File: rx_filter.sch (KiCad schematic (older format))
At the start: 12 parts, among them U10 LM339, U16 TL084

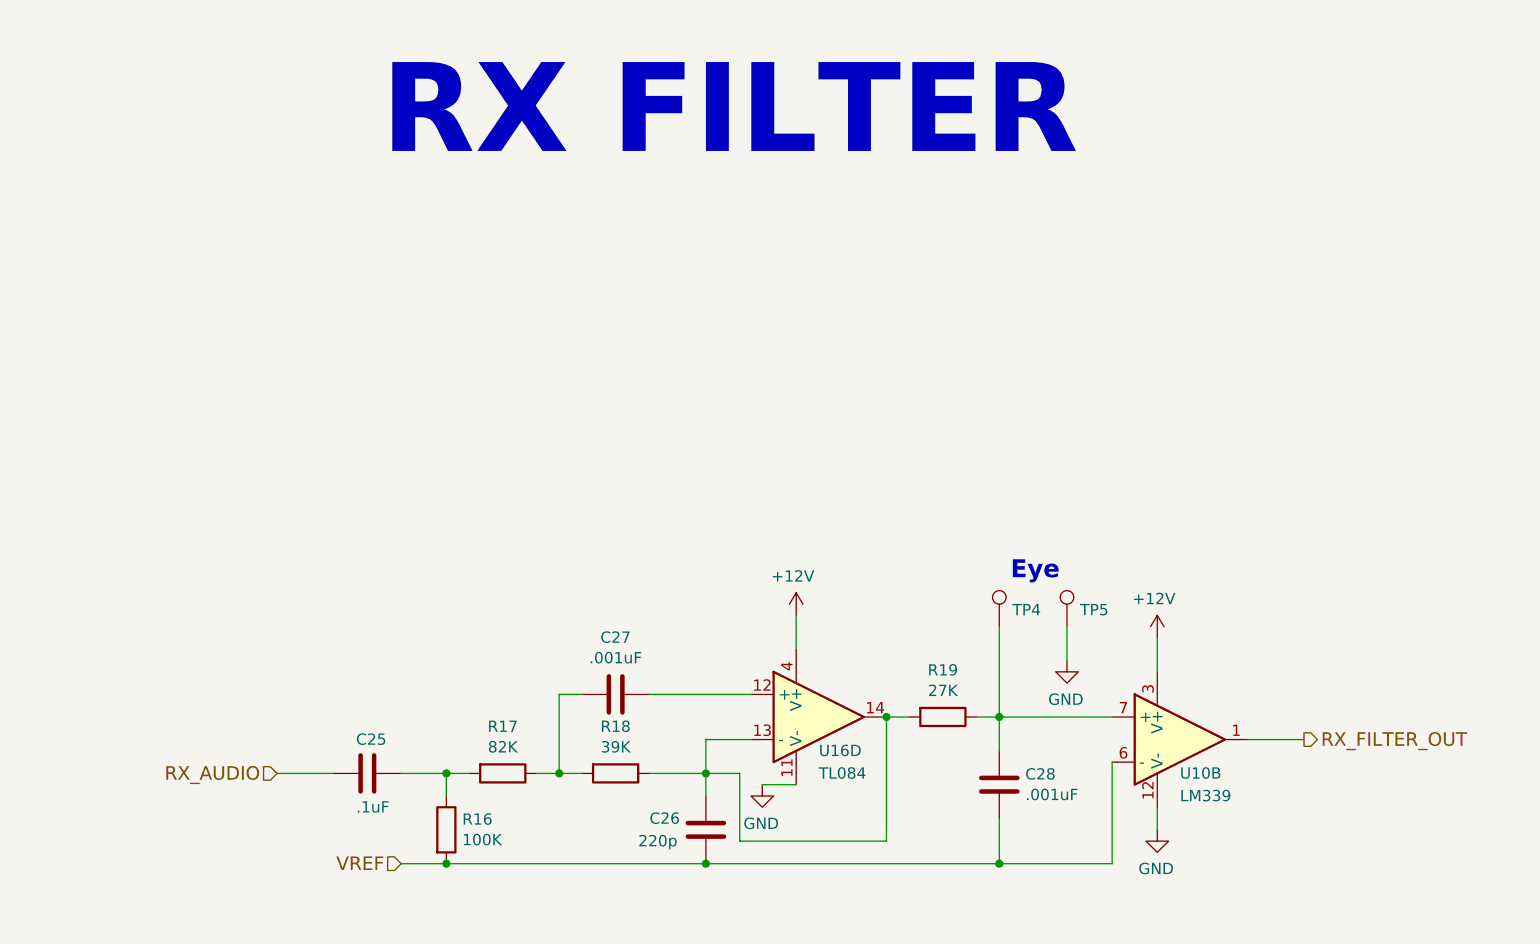
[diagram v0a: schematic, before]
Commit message: Final parts placement and verified net against an actual Issue 3 board.
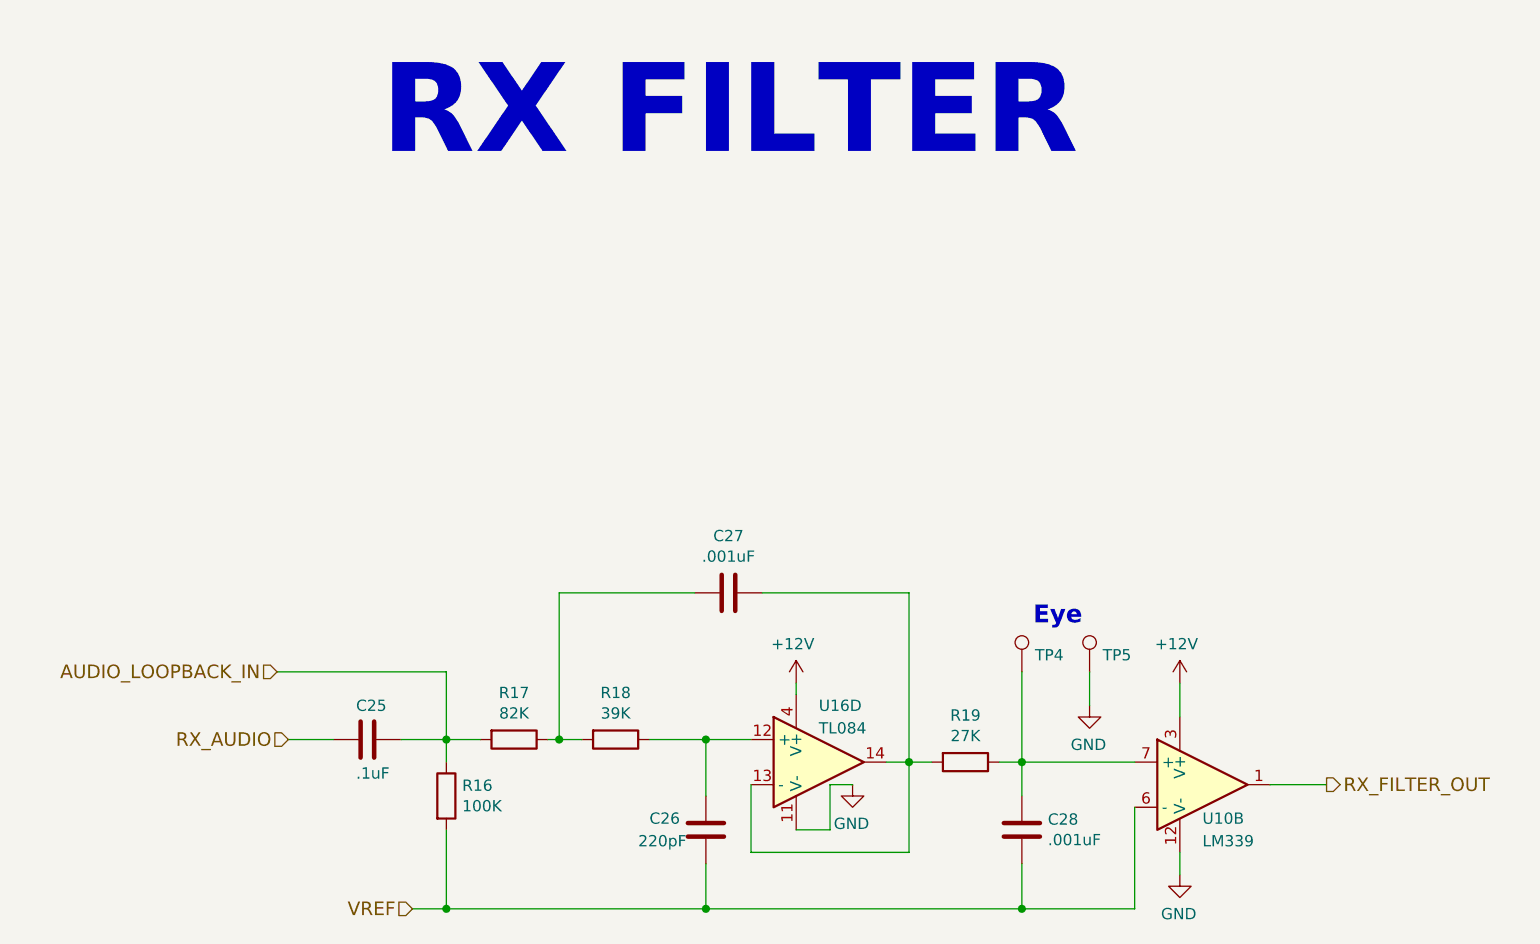
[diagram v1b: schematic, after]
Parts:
- C26: value 220p -> 220pF
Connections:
- net AUDIO_LOOPBACK_IN: now reaches C25.2, R16.1, R17.2
- net at R19.2, U16.13 (-), U16.14: now also C27.2; no longer C26.1, R18.1
- net at U16.12 (+): now also C26.1, R18.1; no longer C27.2
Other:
- moved on the sheet: C25, C27, C28, R16, R17, R18, R19, TP4, TP5, U10B, U16D

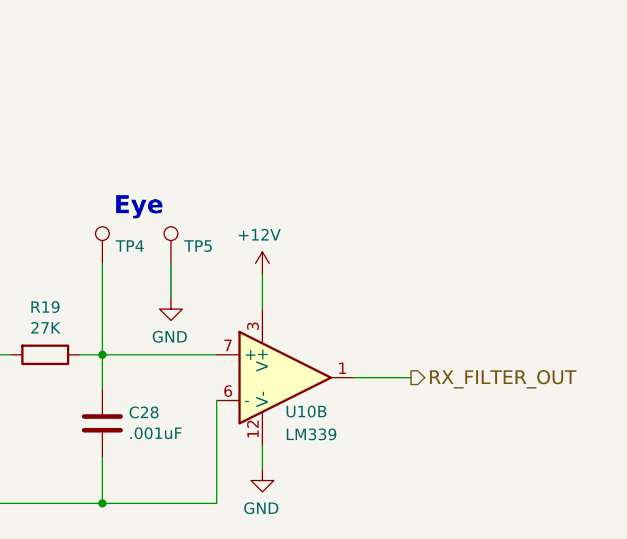
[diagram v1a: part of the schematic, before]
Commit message: Corrected transcription errors.
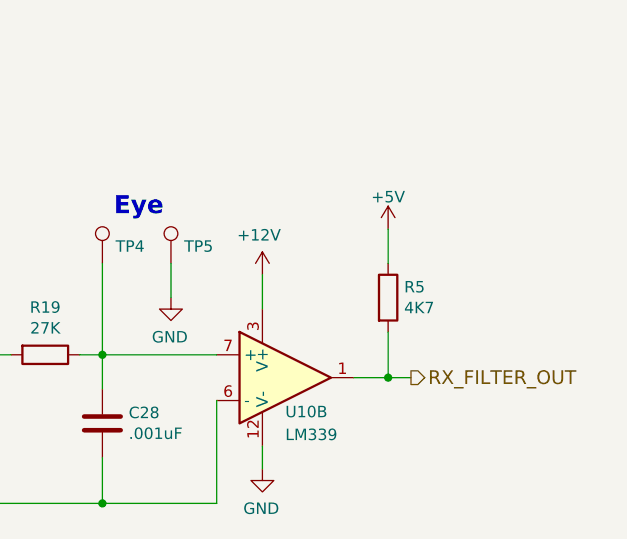
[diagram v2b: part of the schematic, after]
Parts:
- added R5: 4K7, Resistors_THT:R_Axial_DIN0204_L3.6mm_D1.6mm_P7.62mm_Horizontal, symbol R
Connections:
- net RX_FILTER_OUT: now also R5.2
- new net +5V: R5.1
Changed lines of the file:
@@
 	6150 3600 6800 3600
 Connection ~ 4750 5000
+$Comp
+L R R5
+U 1 1 598DADC7
+P 8550 4100
+F 0 "R5" H 8620 4146 50  0000 L CNN
+F 1 "4K7" H 8620 4055 50  0000 L CNN
+F 2 "Resistors_THT:R_Axial_DIN0204_L3.6mm_D1.6mm_P7.62mm_Horizontal" V 8480 4100 50  0001 C CNN
+F 3 "" H 8550 4100 50  0001 C CNN
+	1    8550 4100
+	1    0    0    -1
+$EndComp
+$Comp
+L +5V #PWR?
+U 1 1 598DB144
+P 8550 3800
+F 0 "#PWR?" H 8550 3650 50  0001 C CNN
+F 1 "+5V" H 8550 3940 50  0000 C CNN
+F 2 "" H 8550 3800 50  0001 C CNN
+F 3 "" H 8550 3800 50  0001 C CNN
+	1    8550 3800
+	1    0    0    -1
+$EndComp
+Wire Wire Line
+	8550 4250 8550 4450
+Connection ~ 8550 4450
+Wire Wire Line
+	8550 3950 8550 3800
 $EndSCHEMATC
